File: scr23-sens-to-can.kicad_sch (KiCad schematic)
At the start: 3 parts

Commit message: add TODOs and stuff
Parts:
- added C?: 10uF, symbol Device:C
- added D? (x11): D_TVS, symbol Device:D_TVS
- added D? (x2): LED-GREEN, symbol Device:LED
- added R? (x2): R, symbol Device:R
- added R? (x3): 1k, symbol Device:R
- added U?: AP7370-33Y-13, SOT89_B8D_DIO, symbol scr23-sens-to-can-main:AP7370-33Y-13
- added U?: TPS7A2050PDBVR, DBV0005A-IPC_A, symbol scr23-sens-to-can-main:TPS7A2050PDBVR
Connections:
- net GND: now also J?.11, J?.MH1, J?.MH2, U?.19 (VSSA), C?.2, D?.1 (K), D?.1 (K), D?.2 (A2), D?.2 (A2), D?.2 (A2), D?.2 (A2), D?.2 (A2), D?.2 (A2), D?.2 (A2), D?.2 (A2), D?.2 (A2), D?.2 (A2), D?.2 (A2), R?.2, U?.2 (GND), U?.2 (GND)
- net +3.3V: now reaches U?.21 (VDDA)
- net +3.3V: now also U?.24 (VDD), U?.36 (VDD), U?.48 (VDD), R?.1, U?.1 (VOUT)
- net +12V: now reaches J?.1
- net +12V: now also D?.1 (A1), R?.1, R?.1, U?.3 (VIN)
- net A8: now reaches J?.10
- net A8: now also D?.1 (A1)
- net +5V: now reaches J?.12
- net +5V: now also D?.1 (A1), R?.1, U?.5 (OUT)
- net A0: now reaches J?.2
- net A0: now also D?.1 (A1)
- net A1: now reaches J?.3
- net A1: now also D?.1 (A1)
- net A2: now reaches J?.4
- net A2: now also D?.1 (A1)
- net A3: now reaches J?.5
- net A3: now also D?.1 (A1)
- net A4: now reaches J?.6
- net A4: now also D?.1 (A1)
- net A5: now reaches J?.7
- net A5: now also D?.1 (A1)
- net A6: now reaches J?.8
- net A6: now also D?.1 (A1)
- net A7: now reaches J?.9
- net A7: now also D?.1 (A1)
- new net: R?.1, R?.2, U?.1 (IN)
- new net: D?.2 (A), R?.2 (x2)
- new net: C?.1, R?.2
- new net 5V_EN: U?.3 (EN)
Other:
- note added: "3.3V Regulator 300mA"
- note added: "5V Regulator 300mA"
- note added: "Connector (place TVS near)"
- moved on the sheet: J?, U?A, U?B

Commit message: update pinouts, update uC and add comments/segmentation
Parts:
- added C? (x4): C, symbol Device:C
- added Y?: Crystal 32.768kHz, symbol Device:Crystal
- added Y?: Crystal 4-48MHz, symbol Device:Crystal
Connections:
- net +3.3V: no longer U?.21 (VDDA)
- net A0: now also J?.4; no longer J?.2
- net A1: now also J?.5; no longer J?.3
- net A2: now also J?.6; no longer J?.4
- net A3: now also J?.7; no longer J?.5
- net A4: now also J?.8; no longer J?.6
- net A5: now also J?.9; no longer J?.7
- net A6: now also J?.10; no longer J?.8
- net A7: no longer J?.9
- net A8: no longer J?.10
- net at U?.3 (PC14-OSC32_IN): now also C?.1
- net SWDIO: now reaches U?.37 (PA13)
- net SWCLK: now reaches U?.38 (PA14)
- net at U?.4 (PC15-OSC32_OUT): now also C?.1
- net SWO: now reaches U?.40 (PB3)
- net at U?.5 (PF0-OSC_IN): now also C?.1
- net at U?.6 (PF1-OSC_OUT): now also C?.1
- new net: C?.2, Y?.1 (x2)
- new net: C?.2, Y?.2 (x2)
- new net CANH: J?.2
- new net CANL: J?.3
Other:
- note added: "may not need either of these crystals check AN5093 (G4) and AN2867 (stm32 crystals) --> got someone's advice both probably not need if only sending CAN"

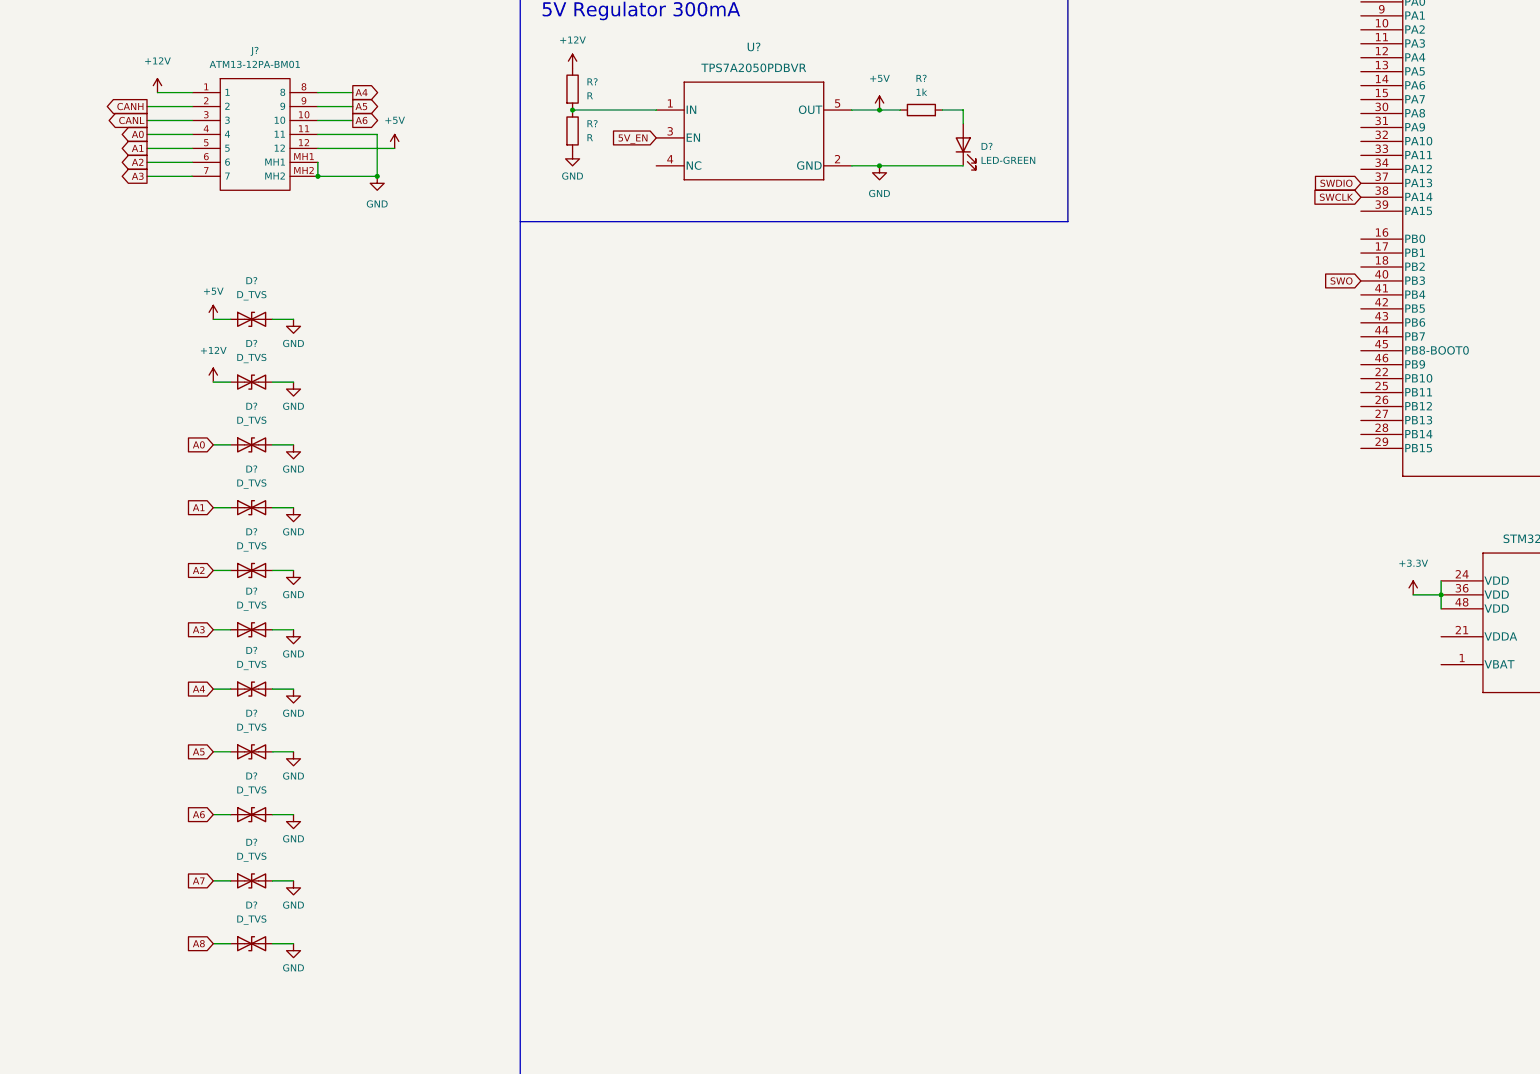
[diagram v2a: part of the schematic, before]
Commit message: add CAN, start 3.3va circuit
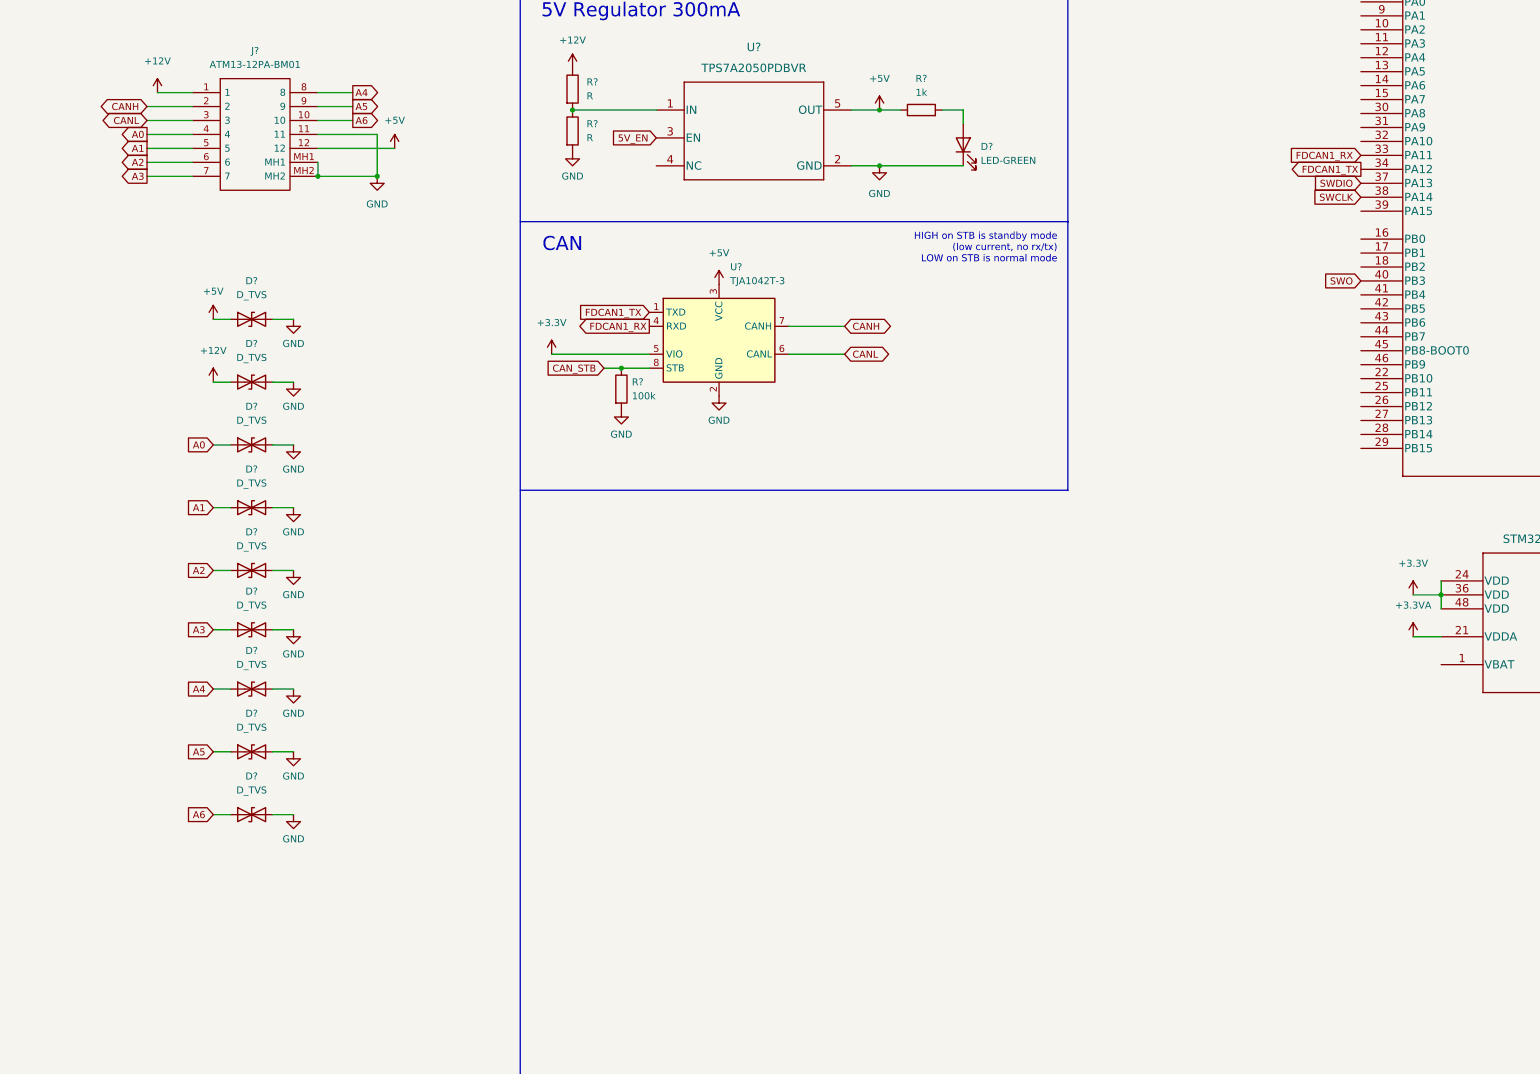
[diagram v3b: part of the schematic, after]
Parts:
- removed D? (x2): D_TVS, symbol Device:D_TVS
- added R?: 100k, symbol Device:R
- added U?: TJA1042T-3, Package_SO:SOIC-8_3.9x4.9mm_P1.27mm, symbol Interface_CAN_LIN:TJA1042T-3
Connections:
- net +3.3V: now also U?.5 (VIO)
- net +5V: now also U?.3 (VCC)
- net CANH: now also U?.7 (CANH)
- net CANL: now also U?.6 (CANL)
- net GND: now also R?.2, U?.2 (GND)
- net FDCAN1_RX: now reaches U?.33 (PA11)
- net FDCAN1_RX: now also U?.4 (RXD)
- net FDCAN1_TX: now reaches U?.34 (PA12)
- net FDCAN1_TX: now also U?.1 (TXD)
- net +3.3VA: now reaches U?.21 (VDDA)
- new net CAN_STB: R?.1, U?.8 (STB)
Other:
- note added: "CAN"
- note added: "HIGH on STB is standby mode (low current, no rx/tx) LOW on STB is normal mode"

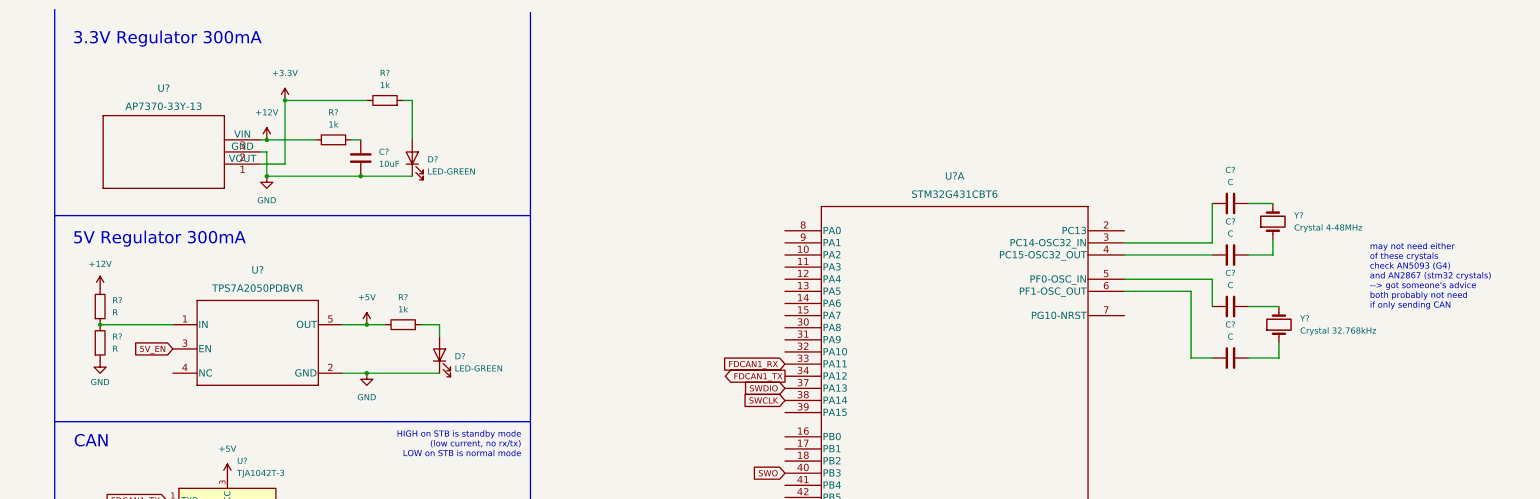
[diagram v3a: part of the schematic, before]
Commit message: idk why so many changes happened but I replaced the 5v LDO with a massive one
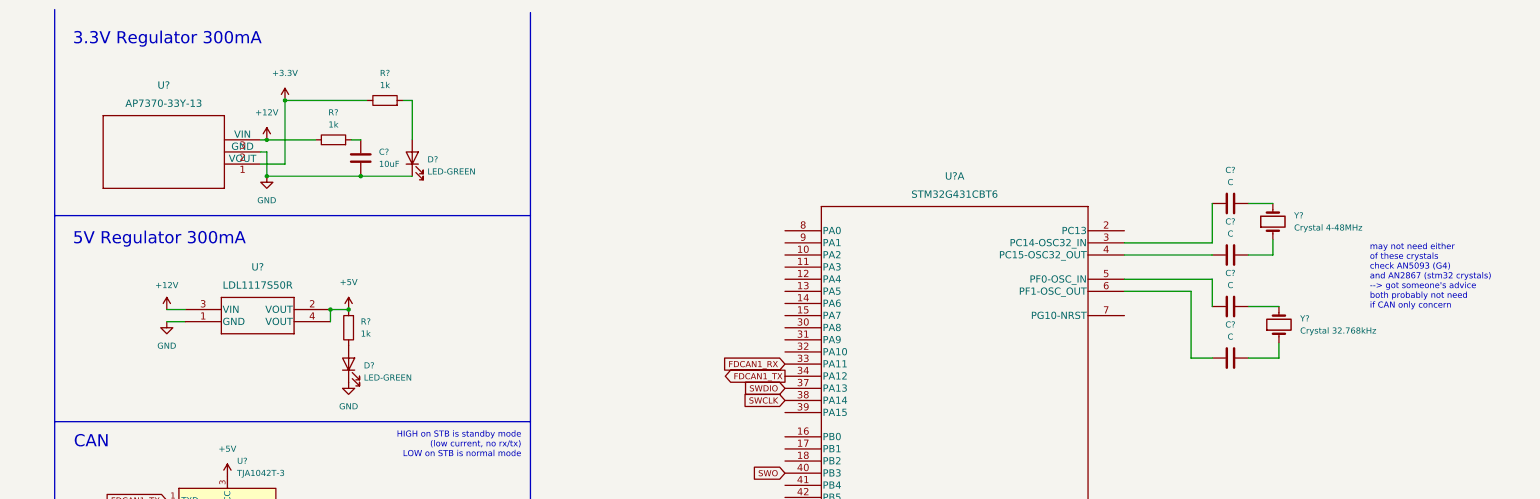
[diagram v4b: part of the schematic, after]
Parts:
- removed R? (x2): R, symbol Device:R
- removed U?: TPS7A2050PDBVR, DBV0005A-IPC_A, symbol scr23-sens-to-can-main:TPS7A2050PDBVR
- added U?: LDL1117S50R, SOT223_STM, symbol scr23-sens-to-can-main:LDL1117S50R
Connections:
- net +12V: now also U?.3 (VIN)
- net +5V: now also R?.2, U?.2 (VOUT), U?.4 (VOUT); no longer R?.1
- net GND: now also U?.1 (GND)
- net at D?.2 (A): now also R?.1; no longer R?.2
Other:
- note added: "may not need either of these crystals check AN5093 (G4) and AN2867 (stm32 crystals) --> got someone's advice both probably not need if CAN only concern"
- note removed: "may not need either of these crystals check AN5093 (G4) and AN2867 (stm32 crystals) --> got someone's advice both probably not need if only sending CAN"
- moved on the sheet: D?, R?

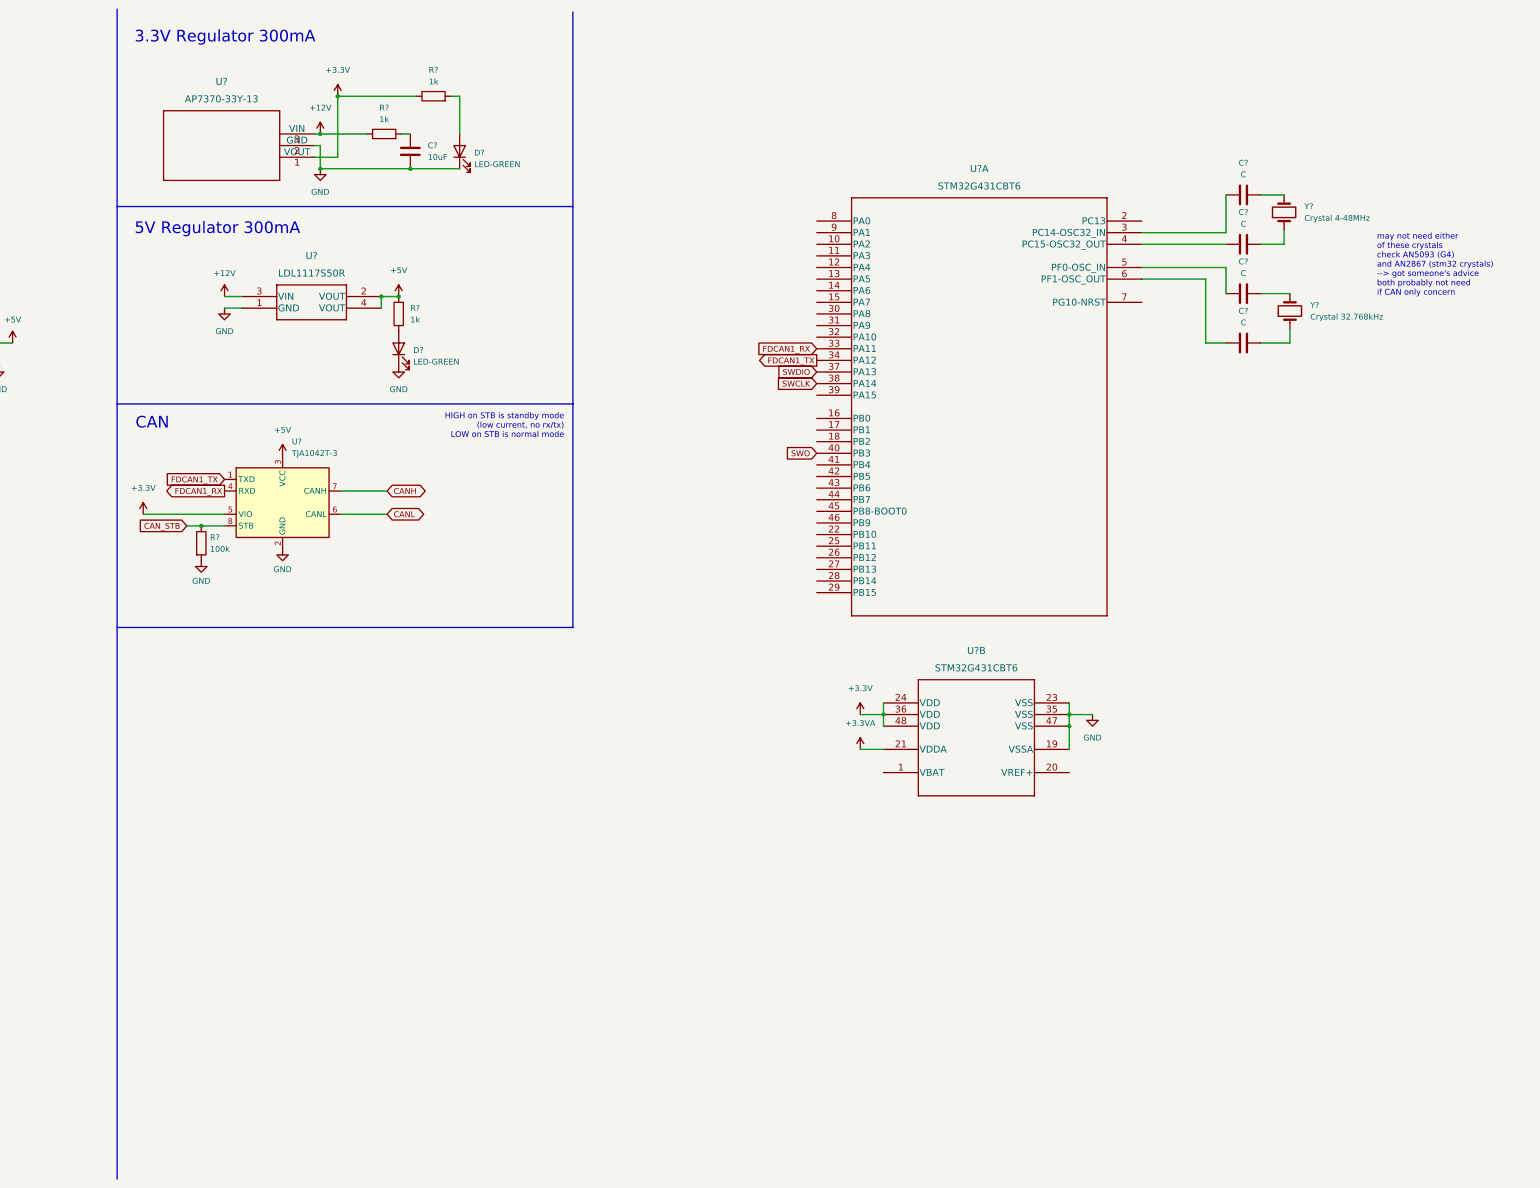
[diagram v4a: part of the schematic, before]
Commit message: pick stm32 adc pins and section out decoupling cap + input buffer area
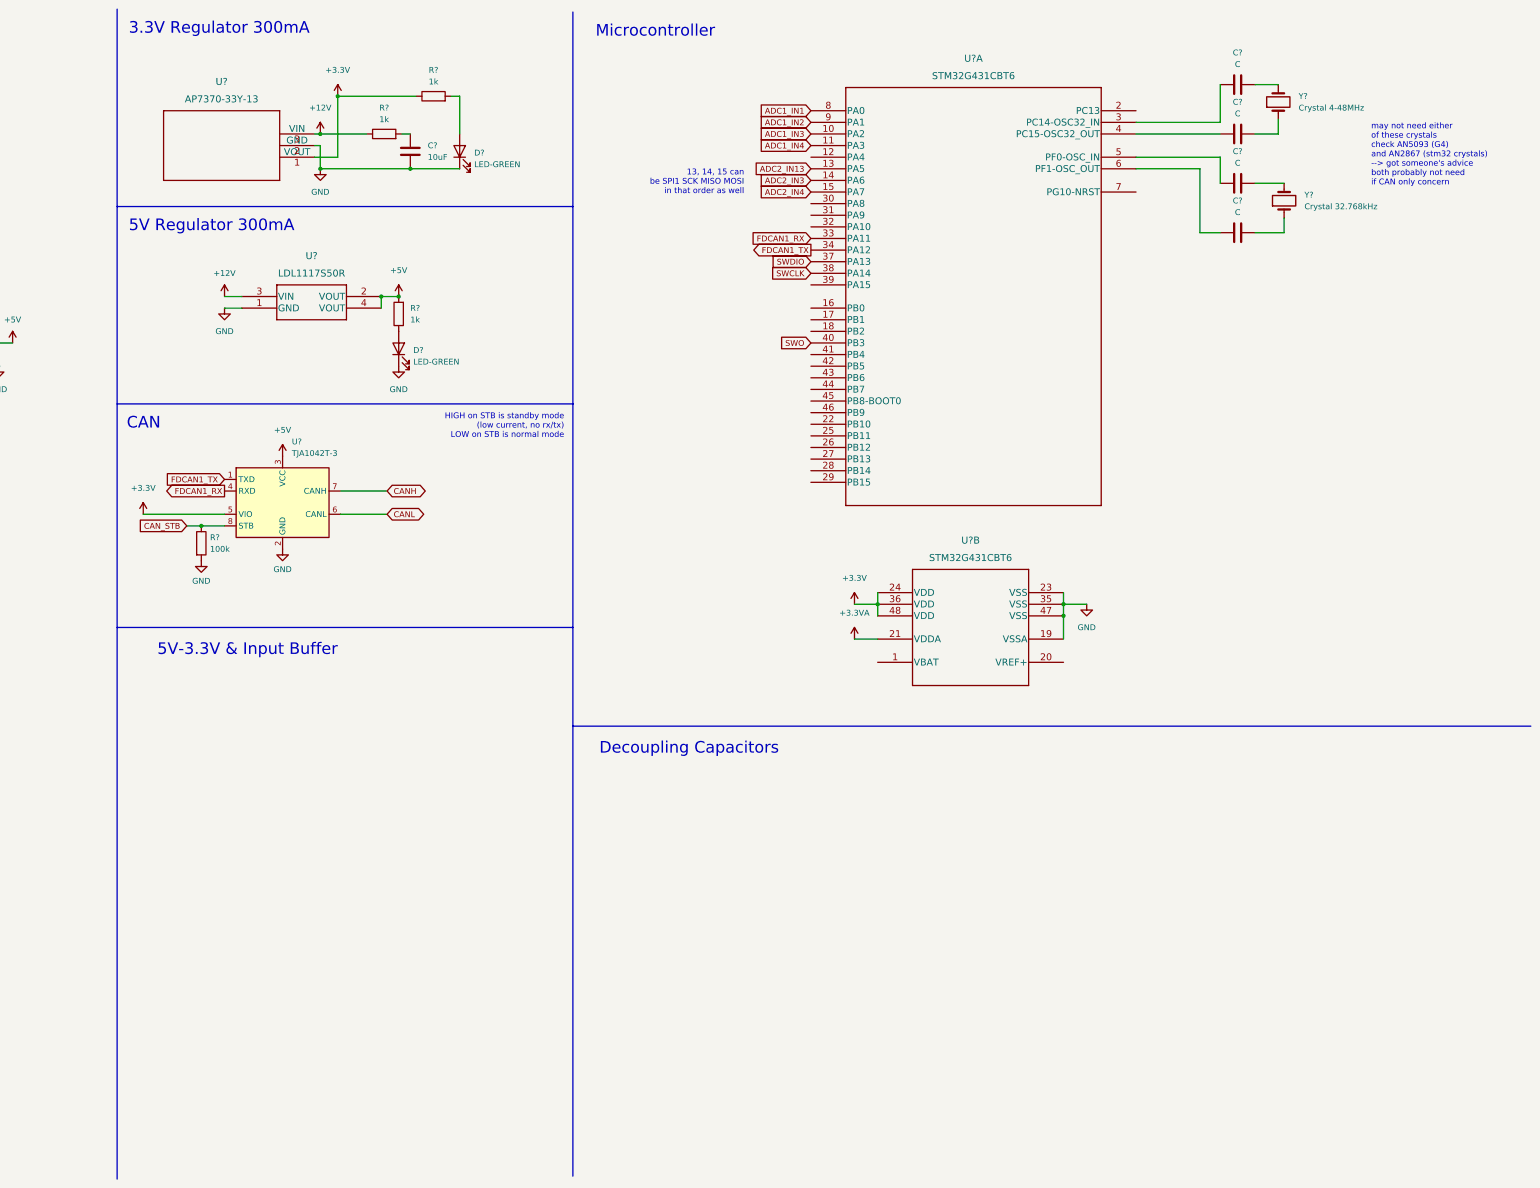
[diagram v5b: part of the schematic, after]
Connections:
- net ADC1_IN3: now reaches U?.10 (PA2)
- net ADC1_IN4: now reaches U?.11 (PA3)
- net ADC2_IN13: now reaches U?.13 (PA5)
- net ADC2_IN3: now reaches U?.14 (PA6)
- net ADC2_IN4: now reaches U?.15 (PA7)
- net ADC1_IN1: now reaches U?.8 (PA0)
- net ADC1_IN2: now reaches U?.9 (PA1)
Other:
- note added: "13, 14, 15 can be SPI1 SCK MISO MOSI in that order as well"
- note added: "5V-3.3V & Input Buffer"
- note added: "Decoupling Capacitors"
- note added: "Microcontroller"
- moved on the sheet: C?, U?A, U?B, Y?

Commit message: change block title
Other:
- note added: "Filtering/Decoupling"
- note removed: "Decoupling Capacitors"
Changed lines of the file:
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@@
     (effects (font (size 2.54 2.54)) (justify right bottom))
   )
-  (text "Decoupling Capacitors" (at 255.27 175.26 180)
+  (text "Filtering/Decoupling\n" (at 250.825 174.625 180)
     (effects (font (size 2.54 2.54)) (justify right bottom))
   )
